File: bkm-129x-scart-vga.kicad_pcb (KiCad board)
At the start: 2 copper layers, 105 x 160 mm, 69 parts, among them J1 DB15_Female_HighDensity_Mount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, J2 SCART-F, J3 SJ1-353XNG, J4 UART, J5 Conn_02x32_Row_Letter_Last, J6 ICSP, Q1 DTC144EKA, Q2 MMBT3904, SW1 PBH4UEENAGX, SW2 PBH4UEENAGX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

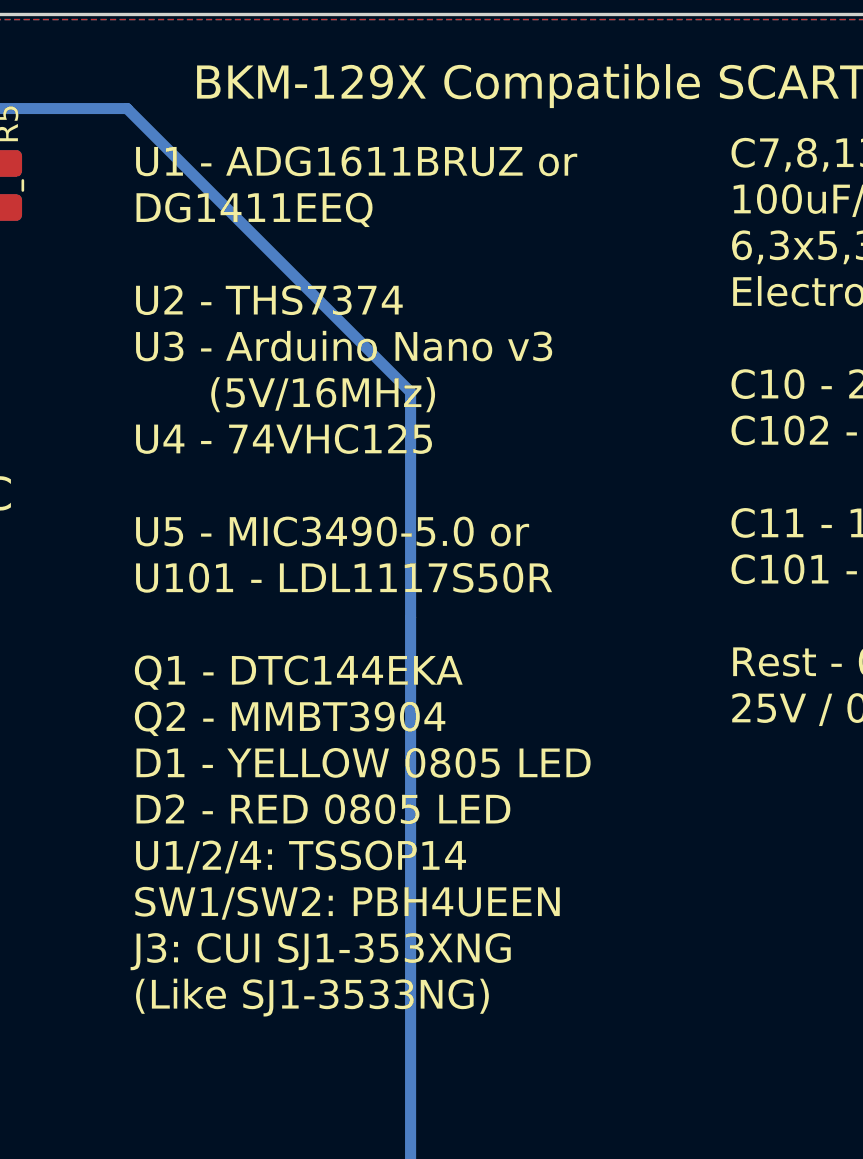
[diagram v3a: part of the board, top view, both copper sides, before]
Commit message: Update PCB silkscreen description.
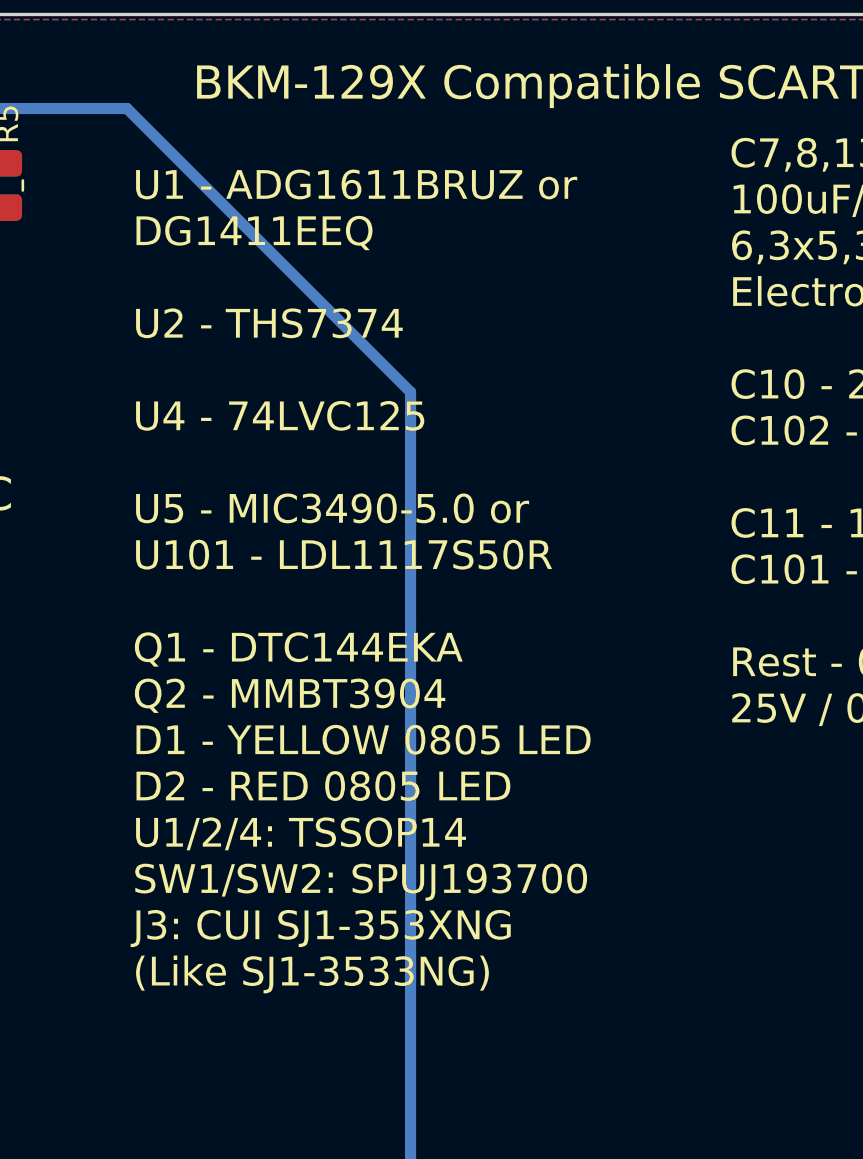
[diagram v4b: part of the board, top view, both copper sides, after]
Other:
- board text added: "U1 - ADG1611BRUZ or DG1411EEQ U2 - THS7374 U4 - 74LVC125 U5 - MIC3490-5.0 or U101 - LDL1117S50R Q1 - DTC144EKA Q2 - MMBT3904 D1 - YELLOW 0805 LED D2 - RED 0805 LED U1/2/4: TSSOP14 SW1/SW2: SPUJ193700 J3: CUI SJ1-353XNG (Like SJ1-3533NG)"
- board text removed: "U1 - ADG1611BRUZ or DG1411EEQ U2 - THS7374 U3 - Arduino Nano v3 (5V/16MHz) U4 - 74VHC125 U5 - MIC3490-5.0 or U101 - LDL1117S50R Q1 - DTC144EKA Q2 - MMBT3904 D1 - YELLOW 0805 LED D2 - RED 0805 LED U1/2/4: TSSOP14 SW1/SW2: PBH4UEEN J3: CUI SJ1-353XNG (Like SJ1-3533NG)"
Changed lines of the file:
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@@
 		)
 	)
-	(gr_text "U1 - ADG1611BRUZ or\nDG1411EEQ\n\nU2 - THS7374\nU3 - Arduino Nano v3\n      (5V/16MHz)\nU4 - 74VHC125\n\nU5 - MIC3490-5.0 or\nU101 - LDL1117S50R\n\nQ1 - DTC144EKA\nQ2 - MMBT3904\nD1 - YELLOW 0805 LED\nD2 - RED 0805 LED\nU1/2/4: TSSOP14\nSW1/SW2: PBH4UEEN\nJ3: CUI SJ1-353XNG\n(Like SJ1-3533NG)"
+	(gr_text "U1 - ADG1611BRUZ or\nDG1411EEQ\n\nU2 - THS7374\n\nU4 - 74LVC125\n\nU5 - MIC3490-5.0 or\nU101 - LDL1117S50R\n\nQ1 - DTC144EKA\nQ2 - MMBT3904\nD1 - YELLOW 0805 LED\nD2 - RED 0805 LED\nU1/2/4: TSSOP14\nSW1/SW2: SPUJ193700\nJ3: CUI SJ1-353XNG\n(Like SJ1-3533NG)"
 		(at 84.0105 50.673 0)
 		(layer "F.SilkS")

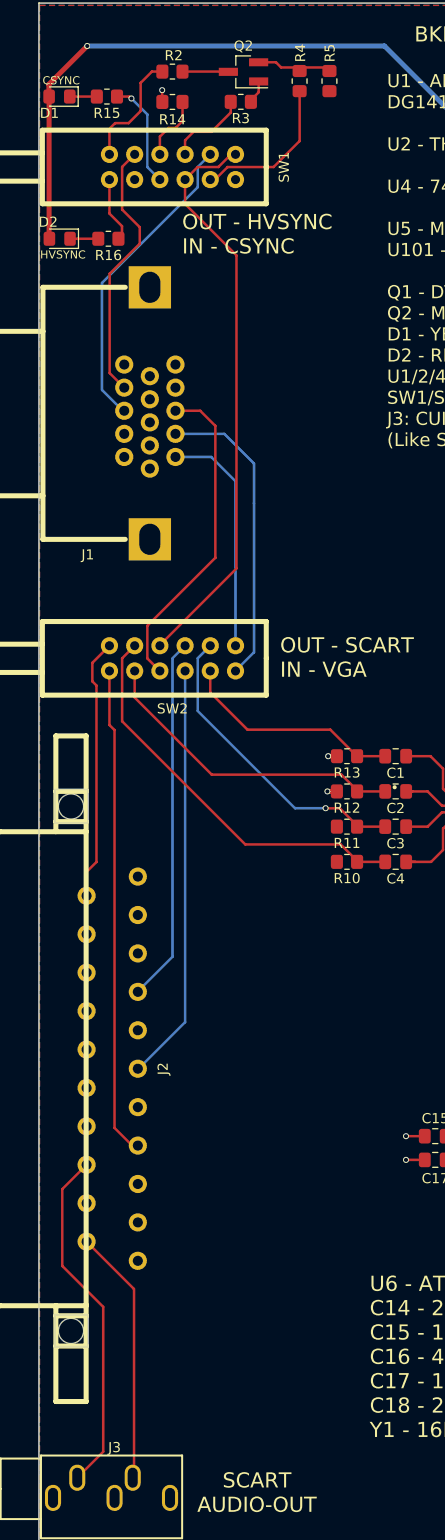
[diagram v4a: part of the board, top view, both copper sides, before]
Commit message: PCB: change input analog RGBS tracks width from 0.25 to 0.35 mm.
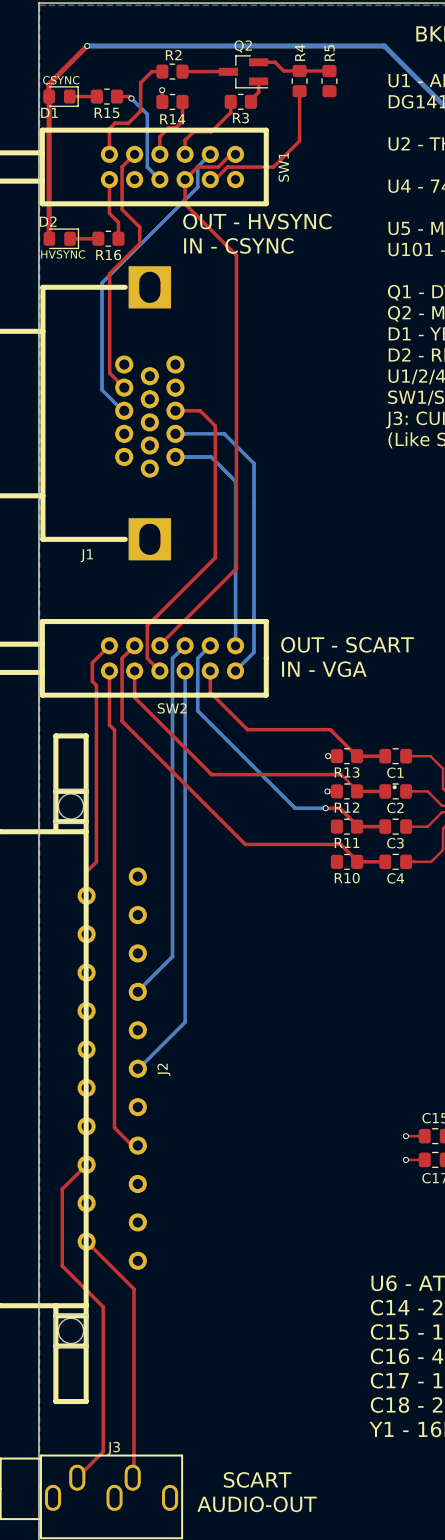
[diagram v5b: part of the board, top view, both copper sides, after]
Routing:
- net /OUT_CS: track 41.0 -> 39.8 mm

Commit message: PCB: fix DRC warnings: update footprints.
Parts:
- J6: footprint Pin_Headers:Pin_Header_Straight_2x03_Pitch2.54mm -> Connector_PinHeader_2.54mm:PinHeader_2x03_P2.54mm_Vertical
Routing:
- net Net-(U2-CH4_IN): track 9.44 -> 8.73 mm
- net +5VD: track 139.0 -> 138.4 mm
